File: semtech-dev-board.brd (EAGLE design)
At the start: 58.1 x 96.4 mm, 58 parts, among them Q1 BSS123, U1 SEMTECH_SX1236, U3 MIC5219 3.3V, X1 BU-SMA-G, X2 BU-SMA-G, X3 BU-SMA-G, X4 BU-SMA-G

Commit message: minor edits
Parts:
- Q2: device crystal:SM49 -> low-gain-radio:CRYSTAL_2.5X2
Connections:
- net N$2: now also Q2.3; no longer Q2.2
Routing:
- net N$2: track 22.9 -> 29.1 mm
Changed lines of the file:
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@@
 <element name="LED1" library="led" package="CHIP-LED0805" value="" x="38.1" y="5.588" rot="R270"/>
 <element name="Q1" library="transistor-small-signal" package="SOT23" value="BSS123" x="42.672" y="10.668" rot="R90"/>
-<element name="Q2" library="crystal" package="SM49" value="" x="27.686" y="32.258" rot="R90">
-<attribute name="MF" value="" x="27.686" y="32.258" size="1.778" layer="27" rot="R90" display="off"/>
-<attribute name="MPN" value="" x="27.686" y="32.258" size="1.778" layer="27" rot="R90" display="off"/>
-<attribute name="OC_FARNELL" value="unknown" x="27.686" y="32.258" size="1.778" layer="27" rot="R90" display="off"/>
-<attribute name="OC_NEWARK" value="unknown" x="27.686" y="32.258" size="1.778" layer="27" rot="R90" display="off"/>
-</element>
+<element name="Q2" library="low-gain-radio" package="CRYSTAL_2.5X2" value="" x="27.686" y="32.258" rot="R90"/>
 <element name="R1" library="rcl" package="M0805" value="" x="37.592" y="10.668" rot="R90"/>
 <element name="R2" library="rcl" package="R0805" value="1k" x="31.496" y="24.13" rot="R180"/>
@@
 <wire x1="43.301" y1="32.784" x2="41.42" y2="32.784" width="0.1524" layer="1"/>
 <wire x1="41.42" y1="32.784" x2="36.068" y2="27.432" width="0.1524" layer="1"/>
-<wire x1="36.068" y1="27.432" x2="27.686" y2="27.432" width="0.1524" layer="1"/>
-<wire x1="27.686" y1="27.432" x2="23.81" y2="29.972" width="0" layer="19" extent="1-1"/>
+<wire x1="36.068" y1="27.432" x2="28.311" y2="31.433" width="0.1524" layer="1"/>
+<wire x1="28.311" y1="31.433" x2="23.81" y2="29.972" width="0" layer="19" extent="1-1"/>
 </signal>
 <signal name="RXTX">
@@
 <signal name="N$2">
 <contactref element="U1" pad="5"/>
-<contactref element="Q2" pad="2"/>
+<contactref element="Q2" pad="3"/>
 <contactref element="C7" pad="1"/>
 <wire x1="43.301" y1="33.434" x2="41.054" y2="33.434" width="0.1524" layer="1"/>
@@
 <wire x1="38.1" y1="30.48" x2="31.242" y2="30.48" width="0.1524" layer="1"/>
 <wire x1="31.242" y1="30.48" x2="27.686" y2="34.036" width="0.1524" layer="1"/>
-<wire x1="27.686" y1="34.036" x2="27.686" y2="37.084" width="0.1524" layer="1"/>
-<wire x1="27.686" y1="37.846" x2="27.686" y2="37.084" width="0.1524" layer="1"/>
-<wire x1="27.686" y1="37.084" x2="27.686" y2="37.846" width="0.1524" layer="1"/>
+<wire x1="27.686" y1="34.036" x2="27.061" y2="33.083" width="0.1524" layer="1"/>
+<wire x1="27.686" y1="37.846" x2="27.061" y2="33.083" width="0.1524" layer="1"/>
+<wire x1="27.061" y1="33.083" x2="27.686" y2="37.846" width="0.1524" layer="1"/>
 <wire x1="23.556" y1="34.036" x2="27.686" y2="34.036" width="0" layer="19" extent="1-1"/>
 </signal>

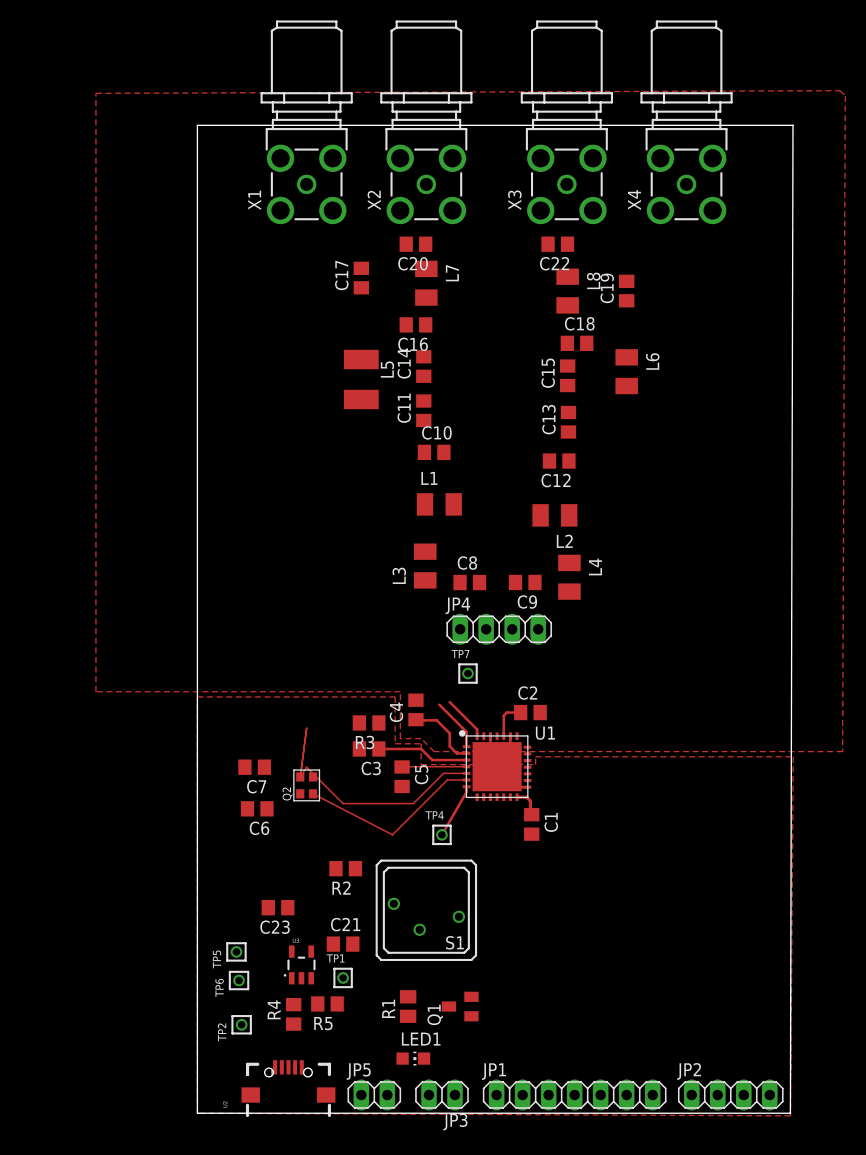
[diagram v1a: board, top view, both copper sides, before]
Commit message: started routing, adjusted placement, named nets
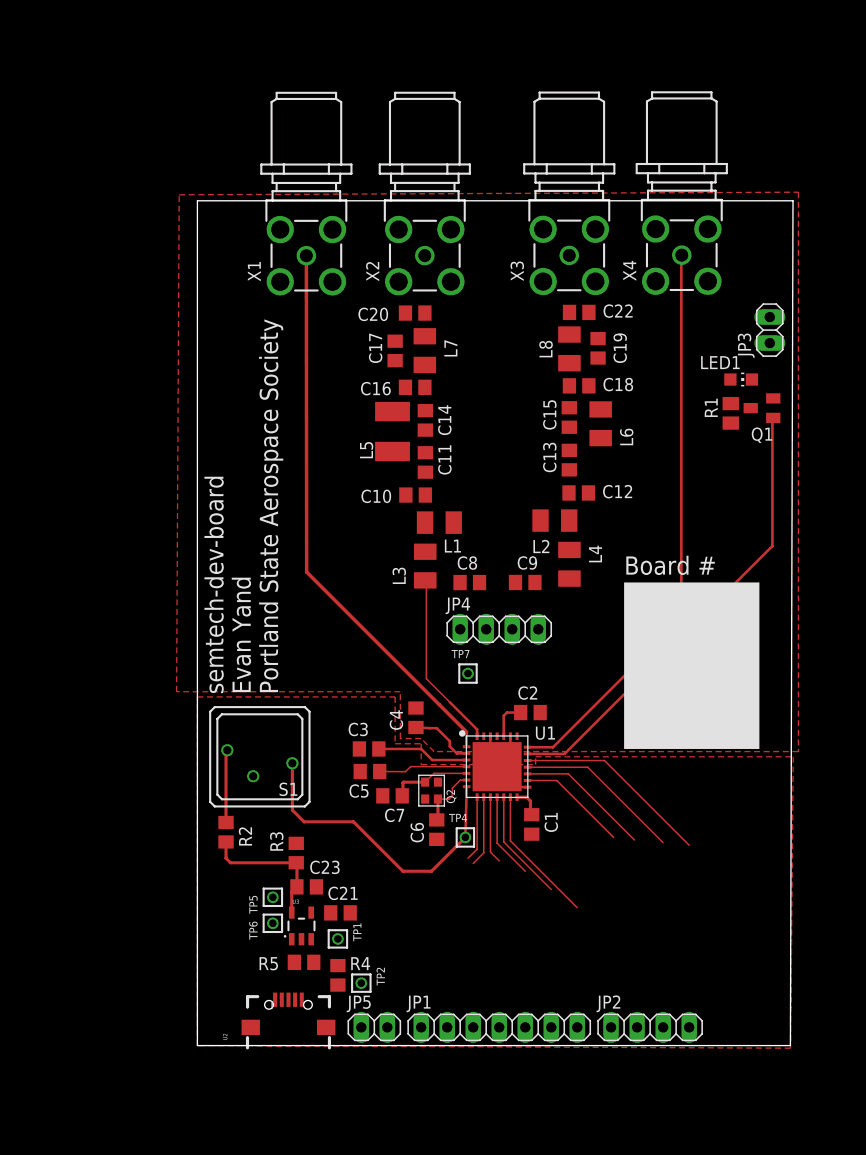
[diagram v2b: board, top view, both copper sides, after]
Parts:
- Q2: value (none) -> 32MHz
- moved JP3 81.2 mm to (72.9, 76.7), turned to 90 degrees
- moved LED1 73.6 mm to (70.1, 71.9)
- moved R1 65.9 mm to (69.1, 68.6), turned to 270 degrees
- moved Q1 65.4 mm to (72.1, 69.1)
- moved S1 22.1 mm to (23.1, 35.1)
- moved C6 17.6 mm to (40.4, 27.9), turned to 270 degrees
- moved R3 14.6 mm to (26.7, 25.7), turned to 270 degrees
- moved C7 13.7 mm to (36.1, 31.2)
- moved TP2 12.4 mm to (33.0, 13.0), turned to 270 degrees
- moved R2 12.2 mm to (19.8, 27.7), turned to 270 degrees
- moved Q2 12.2 mm to (39.9, 31.8)
- moved JP2 10.3 mm to (61.2, 8.64)
- moved JP1 9.89 mm to (46.5, 8.64)
- moved C17 7.84 mm to (36.3, 74.7)
- moved C22 6.98 mm to (54.3, 78.4), turned to 0 degrees
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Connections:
- net N$1 renamed LED-
- net N$15 renamed HFO_PA_HEAD
- net N$2 renamed XTALA
- net N$24 renamed LFO_PA_HEAD
- net N$6 renamed LED+
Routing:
- net RFI_HF: track 0.00 -> 55.7 mm
- net RFI_LF: track 5.20 -> 54.4 mm
- net RXTX: track 0.00 -> 44.9 mm
- net SX1236_RST: track 5.34 -> 30.3 mm
- net XTALA: track 29.1 -> 7.90 mm
- net SPI_NSS: track 0.00 -> 19.2 mm
- net SPI_MOSI: track 0.00 -> 16.3 mm
- net +3V3: track 0.00 -> 13.7 mm
- net DIO5: track 0.00 -> 13.5 mm
- net SPI_MISO: track 0.00 -> 13.1 mm
- net RFO_LF: track 4.43 -> 17.3 mm
- net XTALB: track 18.2 -> 6.10 mm
- net DIO4: track 0.00 -> 10.9 mm
- net SPI_SCK: track 0.00 -> 10.7 mm
- net DIO3: track 0.00 -> 8.37 mm
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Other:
- board size 58.1 x 96.4 mm -> 58.1 x 82.5 mm
- board text added: "Board #"
- board text added: "semtech-dev-board Evan Yand Portland State Aerospace Society"

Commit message: Removed caps
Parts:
- removed C1: 100nF, rcl:C0805
- added C26, C28: 100nF, rcl:C0805
- added C27: 10uF, rcl:C0805
- R5: value (none) -> 0
- moved TP2 1.78 mm to (34.8, 13.0)
- moved R4 1.27 mm to (29.7, 13.0), turned to 180 degrees
- moved R5 0.25 mm to (27.4, 15.2)
- renumbered C3 to C24
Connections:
- net 5219_EN renamed N$1
- net GND: now also C26.2, C27.2, C28.2; no longer C1.2
- net VBAT: now also C26.1; no longer C1.1
- net VREG_IN: now also C27.1, C28.1
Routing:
- net VR_PA: track 0.00 -> 14.8 mm
- net PA_BOOST: track 0.00 -> 6.76 mm
- net HFO_PA_HEAD: track 0.00 -> 6.27 mm
- net LFO_PA_HEAD: track 0.00 -> 6.11 mm
- net VBAT: track 15.6 -> 11.3 mm

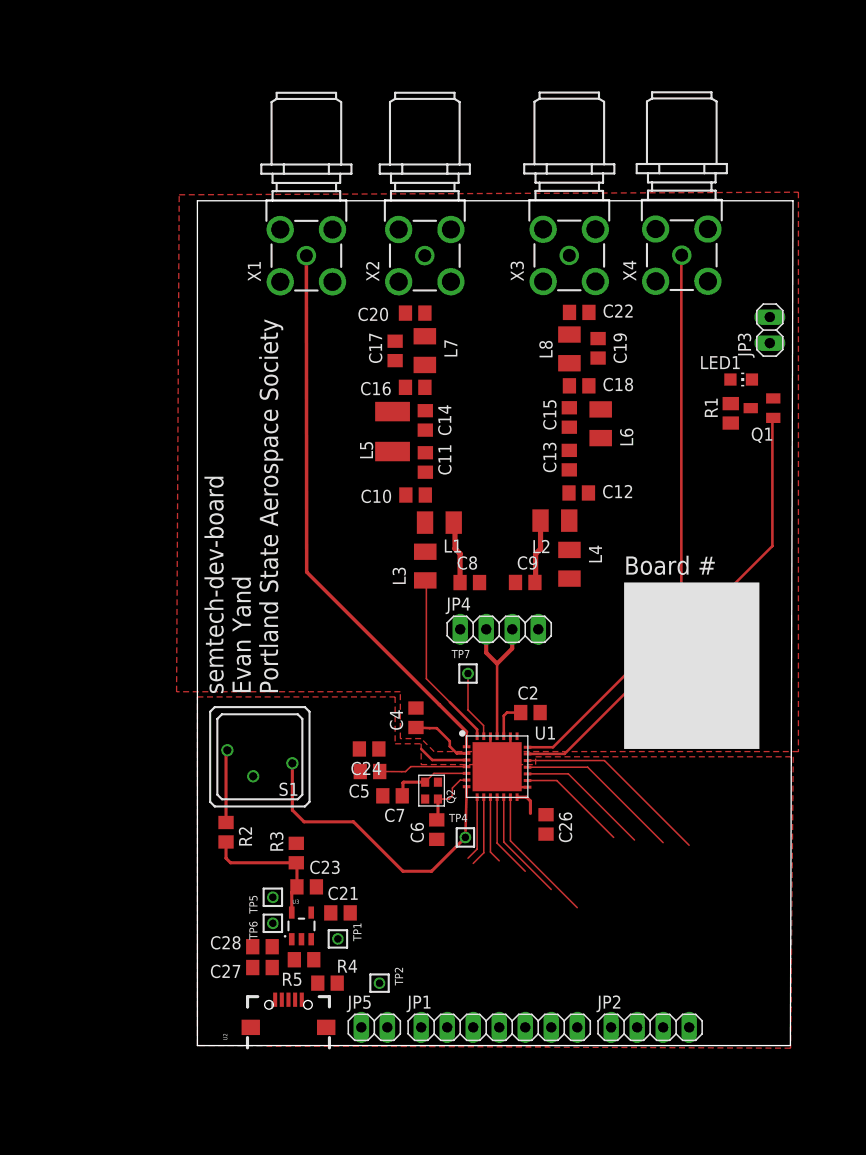
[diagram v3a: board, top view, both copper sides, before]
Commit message: Components placed, 80% routed
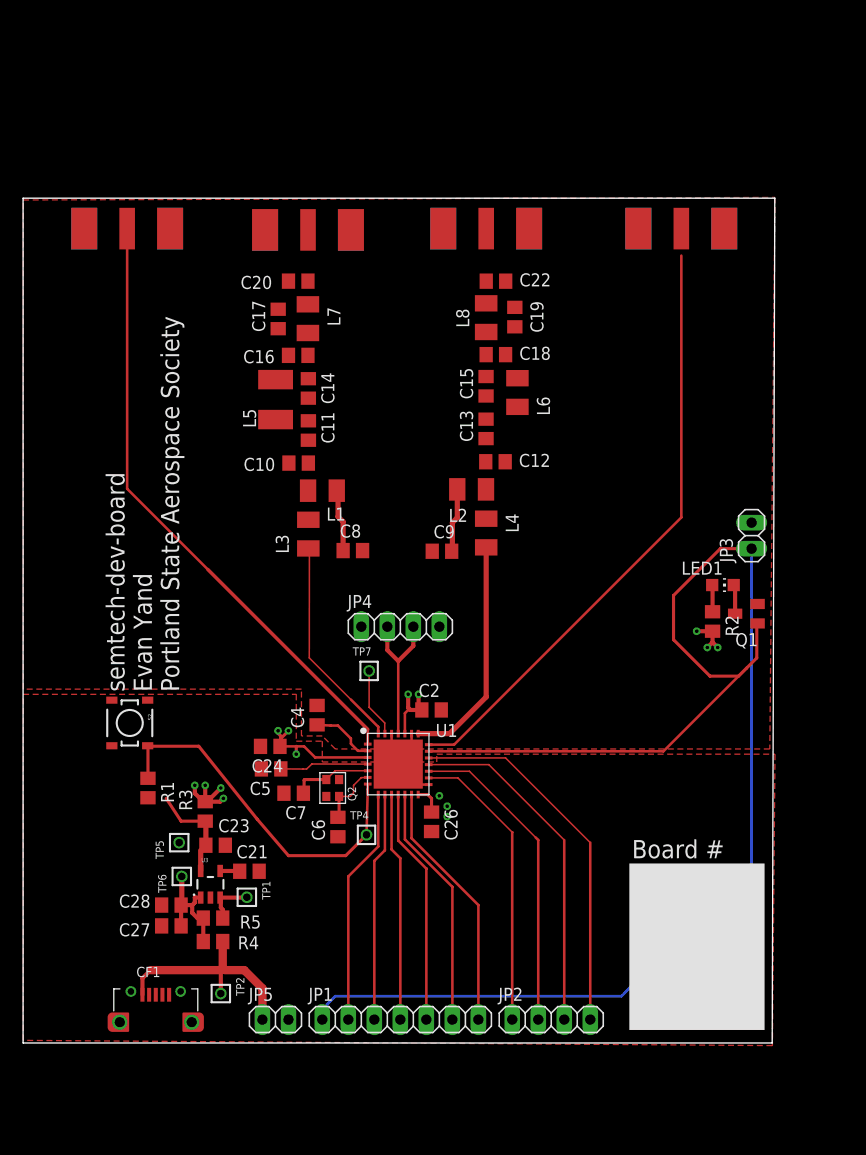
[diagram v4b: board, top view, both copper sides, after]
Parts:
- removed S1: RDT1034, switch:RDT1034
- removed U2: (no value), microusb:USB-MICRO-SMD
- removed X1, X2, X3, X4: BU-SMA-G, con-coax:BU-SMA-G
- added CF1: (no value), psas_c3_team05:USB-MICRO-B-PTH-HIROSE
- added S2: SWITCH-MOMENTARY-2SMD-2, psas_c3_team05:TACTILE_SWITCH_SMD-2
- added U$1, U$2, U$3, U$4: SMAJ716-ND, psas_c3_team05:SMAJ716-ND
- R1: value (none) -> 1k; device rcl:M0805 -> rcl:R0805
- R2: value 1k -> 0
- moved R1 67.6 mm to (12.2, 32.0)
- moved R2 51.8 mm to (67.3, 48.3)
- moved LED1 20.1 mm to (68.3, 51.8)
- moved JP3 20.1 mm to (71.1, 56.6)
- moved Q1 20.1 mm to (70.6, 49.0)
- moved TP2 15.5 mm to (19.3, 11.9)
- moved R4 11.9 mm to (18.5, 17.0)
- moved C11 11.8 mm to (27.9, 66.9)
- moved C17 11.8 mm to (24.9, 77.8)
- moved L3 11.8 mm to (27.8, 56.8)
- moved C10 11.8 mm to (26.9, 63.7)
- moved C16 11.8 mm to (26.9, 74.2)
- moved C20 11.8 mm to (26.9, 81.5)
- moved L1 11.8 mm to (29.2, 61.0)
- moved L7 11.8 mm to (27.8, 77.8)
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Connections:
- removed net RST_SUP: R2.1, S1.A
- net +3V3: no longer R2.2
- net GND: now also CF1.5, S2.2, U$1.GND1, U$1.GND2, U$1.GND3, U$1.GND4, U$2.GND1, U$2.GND2, U$2.GND3, U$2.GND4, U$3.GND1, U$3.GND2, U$3.GND3, U$3.GND4, U$4.GND1, U$4.GND2, U$4.GND3, U$4.GND4; no longer S1.B, U2.GND1, X1.2, X1.3, X1.4, X1.5, X2.2, X2.3, X2.4, X2.5, X3.2, X3.3, X3.4, X3.5, X4.2, X4.3, X4.4, X4.5
- net LED+: now also R2.1; no longer R1.1
- net RFI_HF: now also U$4.P$3; no longer X4.1
- net RFI_LF: now also U$1.P$3; no longer X1.1
- net RFO_HF_OUT: now also U$3.P$3; no longer X3.1
- net RFO_LF_OUT: now also U$2.P$3; no longer X2.1
- net SX1236_RST: now also R1.1, S2.1; no longer S1.A1
- net VBAT: now also R2.2
- net V_IN: now also CF1.1; no longer U2.VBUS1
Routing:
- net RXTX: track 44.9 -> 141.6 mm
- net RFO_HF: track 0.00 -> 22.7 mm
- net V_IN: track 0.00 -> 22.6 mm
- net VBAT: track 11.3 -> 33.9 mm, vias 0 -> 15
- net SPI_SCK: track 10.7 -> 28.6 mm
- net SPI_MISO: track 13.1 -> 31.0 mm
- net SPI_MOSI: track 16.3 -> 33.8 mm
- net SPI_NSS: track 19.2 -> 36.5 mm
- net DIO0: track 6.33 -> 23.2 mm
- net DIO2: track 6.57 -> 22.3 mm
- net DIO1: track 6.90 -> 22.4 mm
- net DIO3: track 8.37 -> 23.1 mm
- net DIO4: track 10.9 -> 23.9 mm
- net VREG_IN: track 0.00 -> 11.8 mm
- net DIO5: track 13.5 -> 24.7 mm
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- added copper zone on layer 2, net VBAT
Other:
- board size 58.1 x 82.5 mm -> 73.4 x 82.5 mm

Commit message: 97% routed, needs vias, mounts, scope clips, and vals
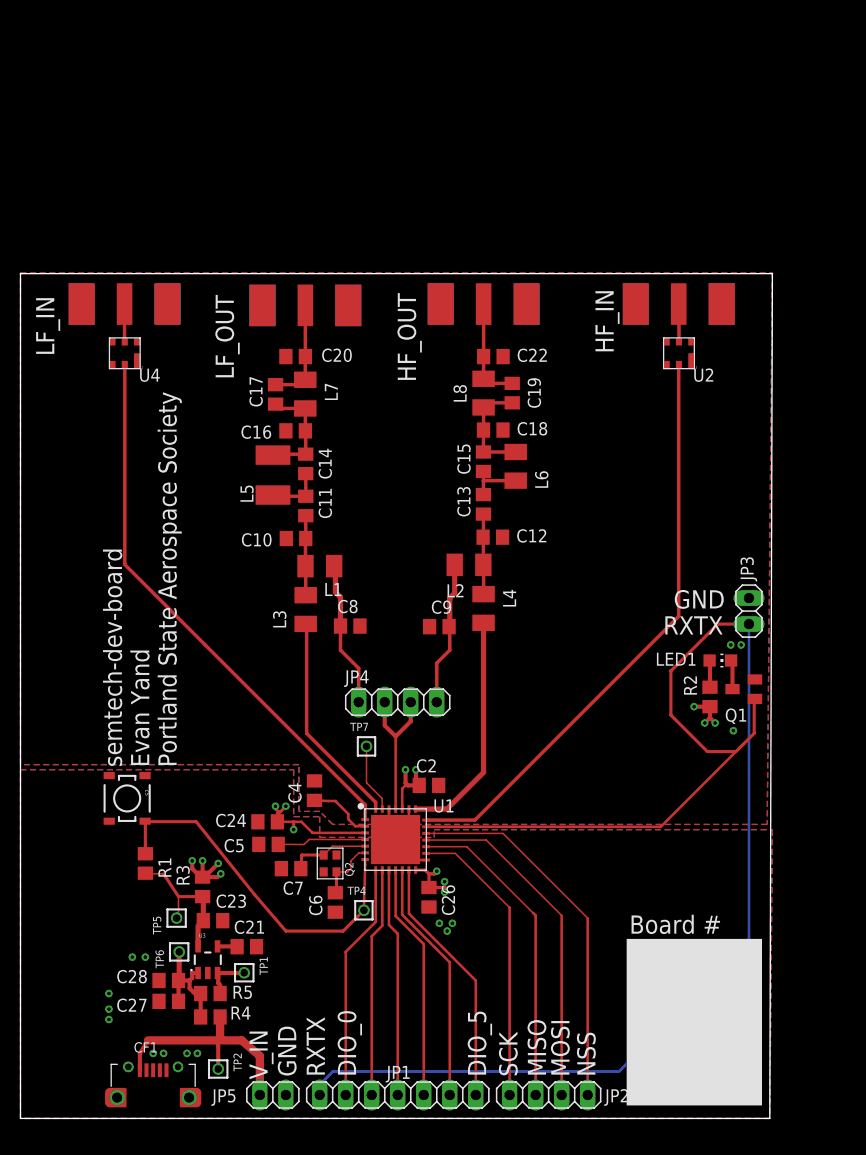
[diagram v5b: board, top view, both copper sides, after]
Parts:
- added U2: QUALCOMM-TDK_B3588, low-gain-radio:DCC6C
- added U4: QUALCOMM-TDK_B3710, low-gain-radio:DCC6C
- moved C19 7.43 mm to (47.8, 70.6)
- moved C11 7.37 mm to (27.6, 59.5)
- moved C13 7.37 mm to (44.9, 59.7)
- moved L5 7.37 mm to (24.4, 62.6)
- moved C26 7.37 mm to (39.6, 21.3)
- moved C5 7.37 mm to (24.0, 26.5)
- moved TP5 7.37 mm to (15.0, 19.3)
- moved C27 7.37 mm to (14.2, 11.2)
- moved C28 7.37 mm to (14.2, 13.2)
- moved R4 7.37 mm to (18.3, 9.65)
- moved U3 7.37 mm to (18.0, 15.2)
- moved TP2 7.37 mm to (19.1, 4.57)
- moved C10 7.37 mm to (26.6, 56.4)
- moved C12 7.37 mm to (45.9, 56.5)
- moved C14 7.37 mm to (27.6, 63.6)
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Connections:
- new net N$5: U$1.P$3, U4.P$5
- new net RFI_HF_ANT: U$4.P$3, U2.P$5
- net GND: now also U2.P$1, U2.P$3, U2.P$4, U2.P$6, U4.P$1, U4.P$3, U4.P$4, U4.P$6
- net RFI_HF: now also U2.P$2; no longer U$4.P$3
- net RFI_LF: now also U4.P$2; no longer U$1.P$3
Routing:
- net RFO_LF_2: track 0.00 -> 10.8 mm
- net RFO_HF_2: track 0.00 -> 10.5 mm
- net RFO_LF_OUT: track 0.00 -> 10.4 mm
- net RFO_HF_OUT: track 0.00 -> 10.3 mm
- net LFO_PA_HEAD: track 6.11 -> 14.3 mm
- net HFO_PA_HEAD: track 6.27 -> 14.2 mm
- net RFO_HF_PA: track 0.00 -> 7.86 mm
- net RFO_LF_PA: track 0.00 -> 7.78 mm
- net RFI_LF: track 60.1 -> 54.1 mm
- net RFO_LF_1: track 0.00 -> 5.46 mm
- net RFO_HF_1: track 0.00 -> 5.42 mm
- net +3V3: track 10.1 -> 14.1 mm
- net RFI_HF_ANT: track 0.00 -> 3.69 mm
- net N$5: track 0.00 -> 3.69 mm
- net VBAT: track 33.9 -> 37.5 mm
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- added copper zone on layer 15, net GND
- added copper zone on layer 16, net GND
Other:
- outline, holes or cut-outs redrawn
- board text added: "DIO_0"
- board text added: "DIO_5"
- board text added: "GND"
- board text added: "HF_IN"
- board text added: "HF_OUT"
- board text added: "LF_IN"
- board text added: "LF_OUT"
- board text added: "MISO"
- board text added: "MOSI"
- board text added: "NSS"
- board text added: "RXTX"
- board text added: "SCK"
- board text added: "V_IN"

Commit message: Filter values updated
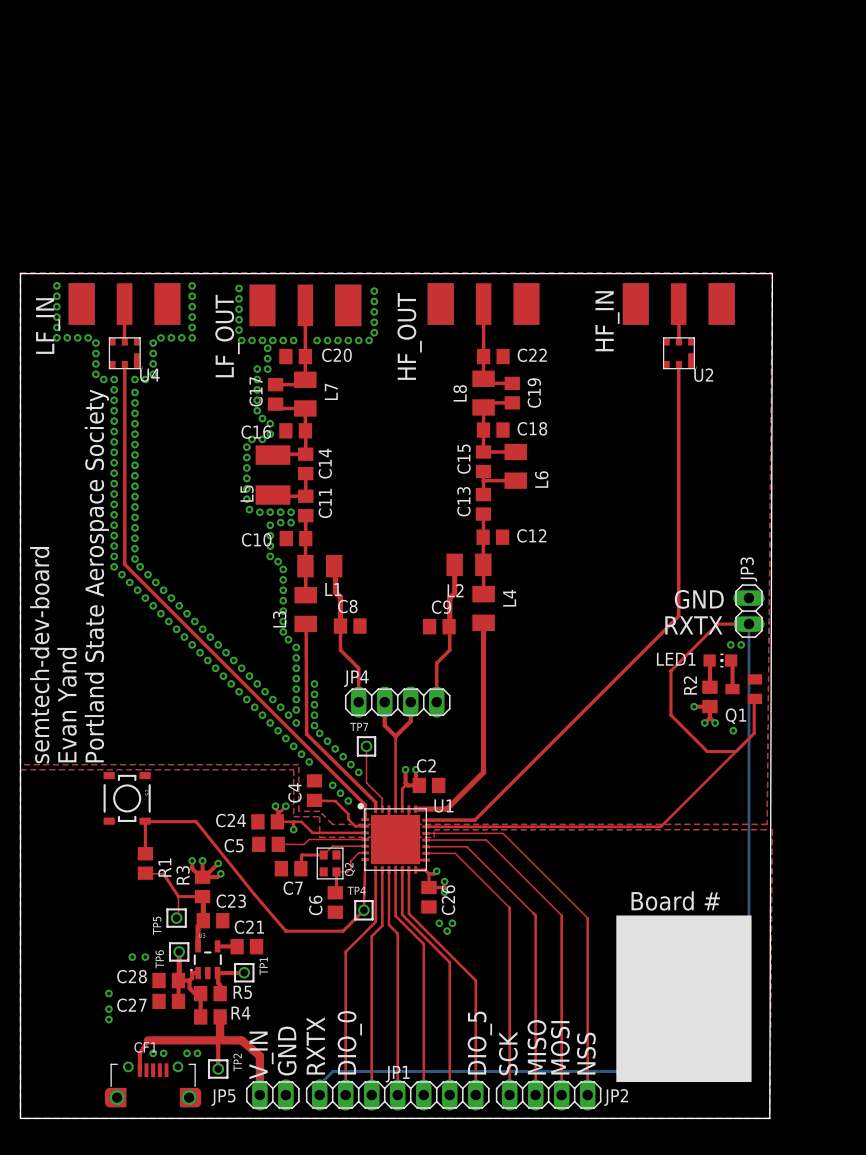
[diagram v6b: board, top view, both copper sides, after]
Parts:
- C10, C16: value 100nF -> 15pF
- C11: value 100nF -> 22pF
- C12: value 100nF -> 4.7pF
- C13, C20: value 100nF -> 8.2pF
- C14: value 100nF -> 2.7pF
- C15, C17, C19: value 100nF -> ??
- C18: value 100nF -> 6.8pF
- C22: value 100nF -> 5.6pF
- C8, C9: value 100nF -> 10nF
- L1, L2: value (none) -> 33nH
- L3, L7: value (none) -> 10nH
- L4: value (none) -> 3.9nH
- L5: value (none) -> 12nH
- L6, L8: value (none) -> 6.8nH
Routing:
- net GND: vias 15 -> 208
